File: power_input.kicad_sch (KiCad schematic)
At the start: 3 parts, among them J1 USB_C_Receptacle_USB2.0_14P

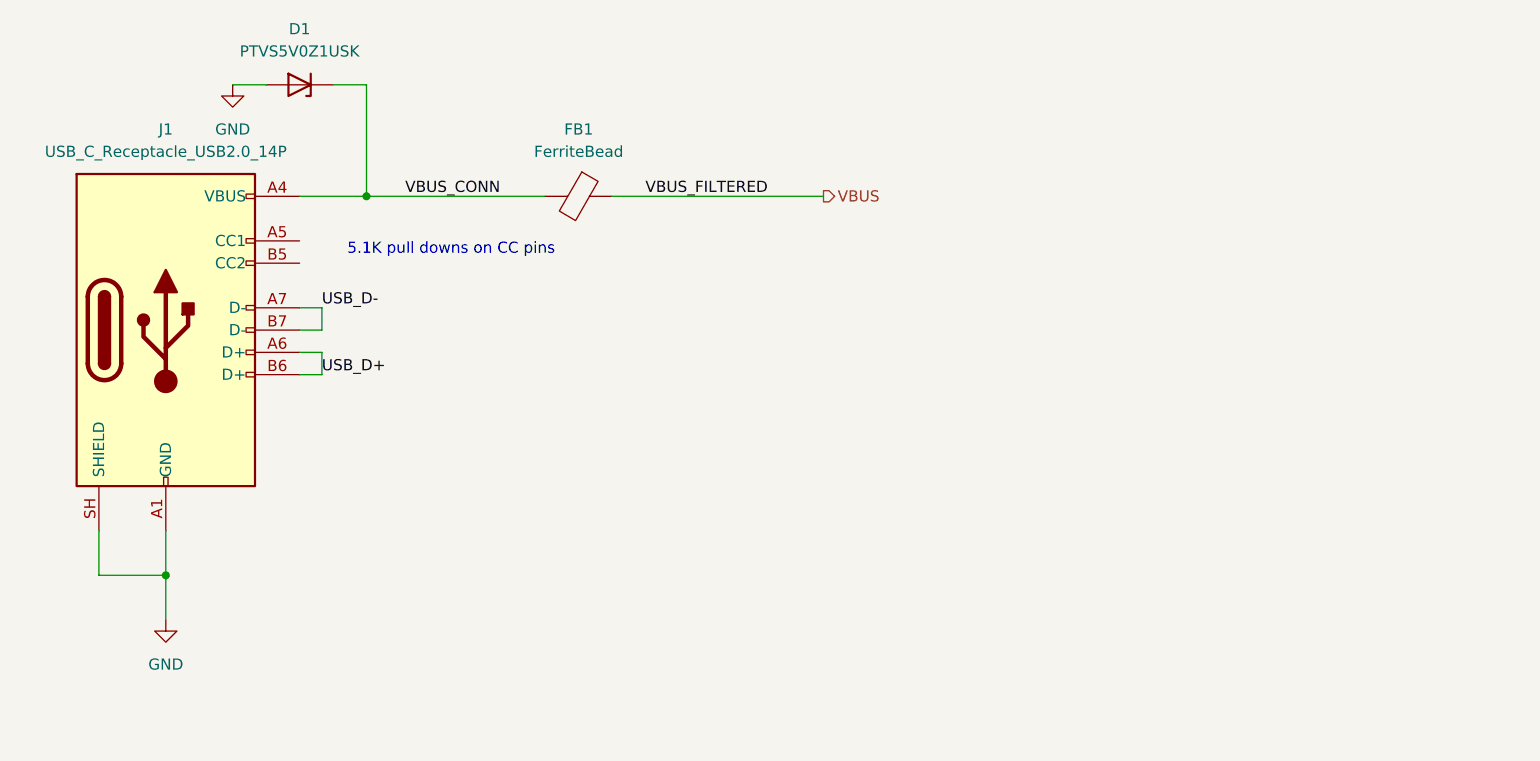
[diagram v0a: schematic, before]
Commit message: Started working on the audio input, including a rough-draft of the first stage.
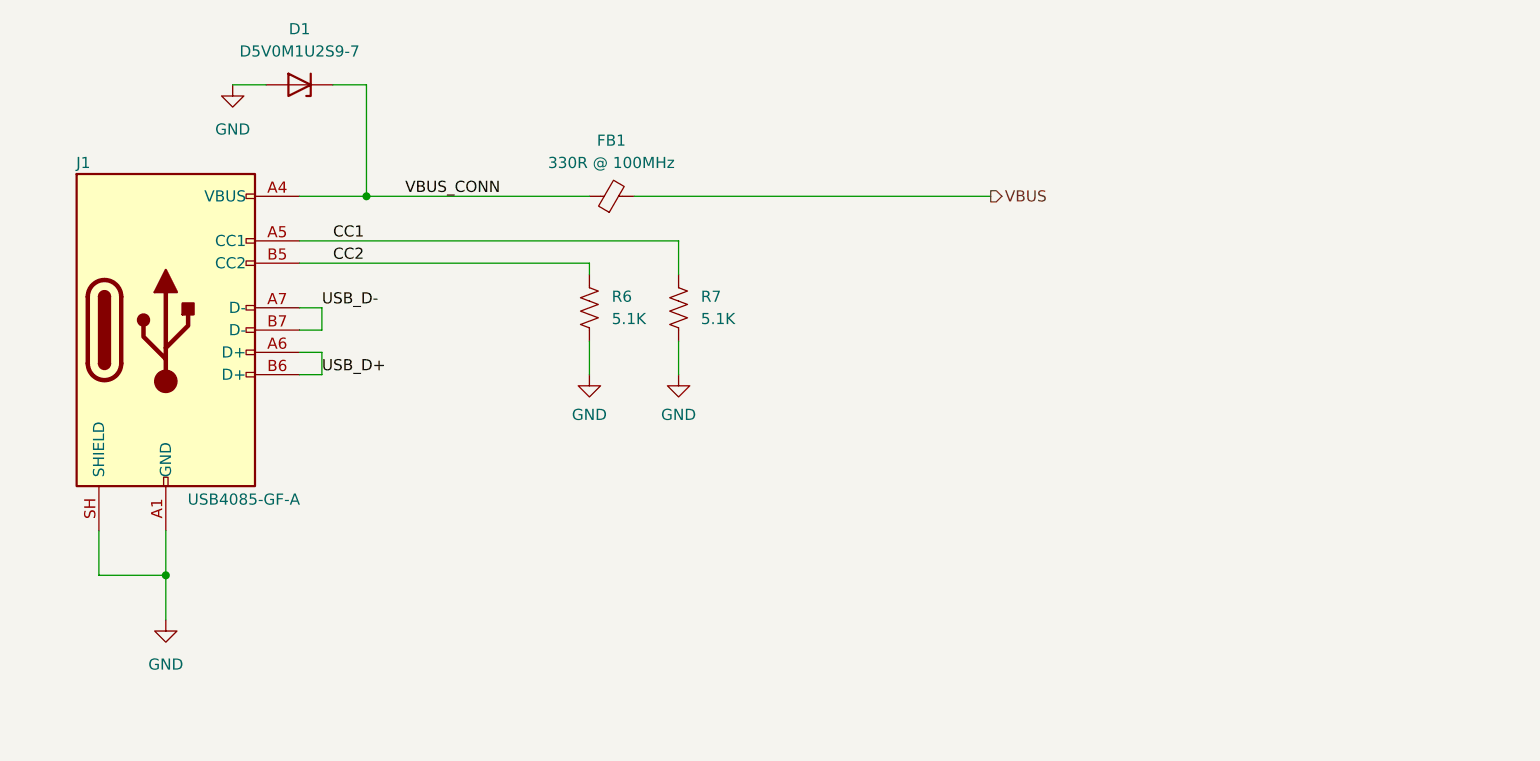
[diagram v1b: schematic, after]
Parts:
- removed FB1: FerriteBead, symbol Device:FerriteBead
- added FB1: 330R @ 100MHz, Inductor_SMD:L_0402_1005Metric, symbol #inventree_kicad:FB_330R_0402_1A2
- added R6, R7: 5.1K, Resistor_SMD:R_0402_1005Metric, symbol #inventree_kicad:R_5K1_0402_1PCT_0W0625
- D1: value PTVS5V0Z1USK -> D5V0M1U2S9-7; footprint Diode_SMD:Nexperia_DSN1608-2_1.6x0.8mm -> Diode_SMD:D_SOD-923; symbol Diode:PTVS5V0Z1USK -> #inventree_kicad:D_TVS_5.5VMM_SOD923; IPN (none) -> 308-0001; InvenTree (none) -> 5; Part URL (none) -> http://10.0.0.33/web/part/5/
- J1: value USB_C_Receptacle_USB2.0_14P -> USB4085-GF-A; symbol Connector:USB_C_Receptacle_USB2.0_14P -> #inventree_kicad:USB_C_USB4085-GF-A; IPN (none) -> 310-0001; InvenTree (none) -> 4; MFG GCT -> (none); PN USB4085-GF-A -> (none); Part URL (none) -> http://10.0.0.33/web/part/4/
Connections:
- net GND: now also R6.2, R7.2
- net VBUS: now also FB1.2
- net VBUS_CONN: now also FB1.1
- net CC1: now reaches J1.A5 (CC1)
- net CC1: now also R7.1
- net CC2: now reaches J1.B5 (CC2)
- net CC2: now also R6.1
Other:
- note removed: "5.1K pull downs on CC pins"

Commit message: Implemented boost stage and now working on schematics for current buffers and rail splitter.
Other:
- title: (none) -> ${PROJECT_NAME}
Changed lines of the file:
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@@
 	(generator_version "10.0")
 	(paper "A4")
+	(title_block
+		(title "${PROJECT_NAME}")
+		(date "2026-08-25")
+		(rev "${REVISION}")
+		(comment 1 "${PCBA_IPN}")
+	)
 	(junction
 		(at 53.34 118.11)

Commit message: First rough draft of schematics complete -- missing a lot of PLM/Inventree work. Ran through several Claude reviews.
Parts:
- added C33: TCJA106M016R0200, symbol Device:C_Polarized_US
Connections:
- net GND: now also C33.2
- net VBUS: now also C33.1
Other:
- moved on the sheet: D1, FB1, J1, R6, R7

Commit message: Started adding some 3D models and footprints.
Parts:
- J1: symbol #inventree_kicad:USB_C_USB4085-GF-A -> connectors:USB_C_USB4085-GF-A
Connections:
- no-connect marks 0 -> 2
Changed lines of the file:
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@@
 		(color 0 0 0 0)
+	)
+	(no_connect
+		(at 119.38 111.76)
+	)
+	(no_connect
+		(at 119.38 109.22)
 	)
 	(wire
@@
 	)
 	(symbol
-		(lib_id "#inventree_kicad:USB_C_USB4085-GF-A")
+		(lib_id "connectors:USB_C_USB4085-GF-A")
 		(at 104.14 97.79 0)
 		(unit 1)
@@
 		(pin "SH"
 		)
+		(pin "B8"
+		)
+		(pin "A8"
+		)
 		(instances

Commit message: Picked off the board parts and ordered on DigiKey -- also added notes on schematic.
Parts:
- C33: footprint (none) -> polymers:TCJA_AVX
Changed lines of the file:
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@@
 			)
 		)
-		(property "Footprint" ""
+		(property "Footprint" "polymers:TCJA_AVX"
 			(at 182.88 93.98 0)
 			(hide yes)

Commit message: Finilizing DRC and ERC
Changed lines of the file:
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@@
+	)
+	(junction
+		(at 189.23 82.55)
+		(diameter 0)
+		(color 0 0 0 0)
 	)
 	(junction
@@
 	(wire
 		(pts
+			(xy 189.23 78.74) (xy 189.23 82.55)
+		)
+		(stroke
+			(width 0)
+			(type default)
+		)
+	)
+	(wire
+		(pts
 			(xy 119.38 82.55) (xy 127 82.55)
 		)
@@
 	(wire
 		(pts
-			(xy 182.88 82.55) (xy 198.12 82.55)
+			(xy 182.88 82.55) (xy 189.23 82.55)
 		)
 		(stroke
@@
 		(pts
 			(xy 127 82.55) (xy 152.4 82.55)
+		)
+		(stroke
+			(width 0)
+			(type default)
+		)
+	)
+	(wire
+		(pts
+			(xy 189.23 82.55) (xy 198.12 82.55)
 		)
 		(stroke
@@
 					(unit 1)
 				)
+			)
+		)
+	)
+	(symbol
+		(lib_id "power:PWR_FLAG")
+		(at 189.23 78.74 0)
+		(unit 1)
+		(body_style 1)
+		(exclude_from_sim no)
+		(in_bom yes)
+		(on_board yes)
+		(in_pos_files yes)
+		(dnp no)
+		(property "Reference" "#FLG01"
+			(at 189.23 76.835 0)
+			(hide yes)
+			(show_name no)
+			(do_not_autoplace no)
+			(effects
+				(font
+					(size 1.27 1.27)
+				)
+			)
+		)
+		(property "Value" "PWR_FLAG"
+			(at 189.23 74.93 0)
+			(show_name no)
+			(do_not_autoplace no)
+			(effects
+				(font
+					(size 1.27 1.27)
+				)
+			)
+		)
+		(property "Footprint" ""
+			(at 189.23 78.74 0)
+			(hide yes)
+			(show_name no)
+			(do_not_autoplace no)
+			(effects
+				(font
+					(size 1.27 1.27)
+				)
+			)
+		)
+		(property "Datasheet" ""
+			(at 189.23 78.74 0)
+			(hide yes)
+			(show_name no)
+			(do_not_autoplace no)
+			(effects
+				(font
+					(size 1.27 1.27)
+				)
+			)
+		)
+		(property "Description" "Special symbol for telling ERC where power comes from"
+			(at 189.23 78.74 0)
+			(hide yes)
+			(show_name no)
+			(do_not_autoplace no)
+			(effects
+				(font
+					(size 1.27 1.27)
+				)
+			)
+		)
+		(pin "1"
+		)
+		(instances
+			(project "headphone_amp"
+				(path "/62ffec33-ae93-49a8-bfe6-566578dd8e82/14462d11-f69f-4768-a94b-e7cc4b589cf9"
+					(reference "#FLG01")
+					(unit 1)
+				)

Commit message: Finally updated all parts in InvenTree and linked them with KiCAD. Ready for BOM exports to JLC.
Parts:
- C33: value TCJA106M016R0200 -> 10uF; symbol Device:C_Polarized_US -> inventree_kicad:C_10U_TA_POLY_16V_1206; IPN (none) -> 301-0017; InvenTree (none) -> 51; Part URL (none) -> http://10.0.0.33/web/part/51/
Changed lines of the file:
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@@
 	)
 	(symbol
-		(lib_id "Device:C_Polarized_US")
+		(lib_id "inventree_kicad:C_10U_TA_POLY_16V_1206")
 		(at 182.88 93.98 0)
 		(unit 1)
@@
 			)
 		)
-		(property "Value" "TCJA106M016R0200"
+		(property "Value" "10uF"
 			(at 186.69 94.6149 0)
 			(show_name no)
@@
 			)
 		)
-		(property "Description" "Polarized capacitor, US symbol"
+		(property "Description" "10 µF ±20% 16V Molded Tantalum Polymer Capacitor 1206 (3216 Metric) 200mOhm"
 			(at 182.88 93.98 0)
 			(hide yes)
+			(show_name no)
+			(do_not_autoplace no)
+			(effects
+				(font
+					(size 1.27 1.27)
+				)
+			)
+		)
+		(property "InvenTree" "51"
+			(at 182.88 93.98 0)
+			(hide yes)
+			(show_name no)
+			(do_not_autoplace no)
+			(effects
+				(font
+					(size 1.27 1.27)
+				)
+			)
+		)
+		(property "Part URL" "http://10.0.0.33/web/part/51/"
+			(at 182.88 93.98 0)
+			(hide yes)
+			(show_name no)
+			(do_not_autoplace no)
+			(effects
+				(font
+					(size 1.27 1.27)
+				)
+			)
+		)
+		(property "IPN" "301-0017"
+			(at 182.88 93.98 0)
+			(hide yes)
